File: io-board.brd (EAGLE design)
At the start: 76.2 x 75.9 mm, 26 parts

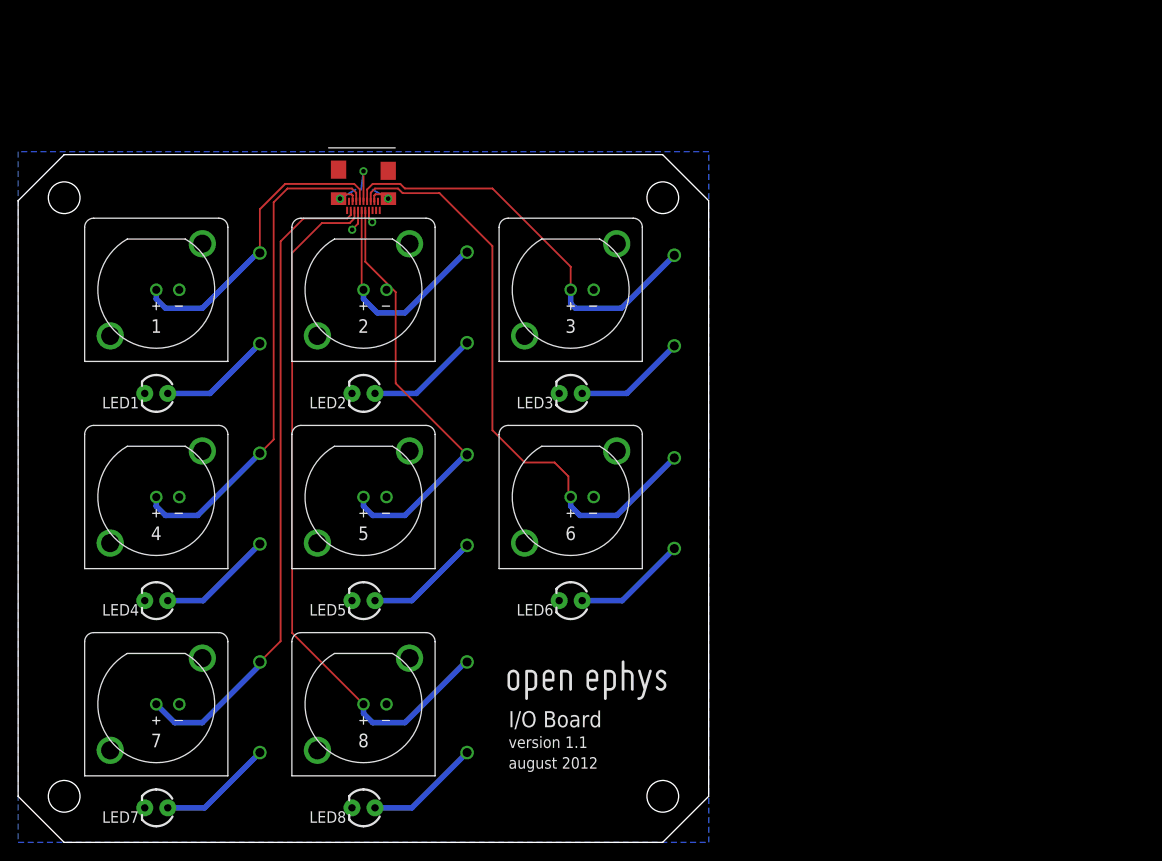
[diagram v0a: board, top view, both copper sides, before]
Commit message: Make rackmount board the default
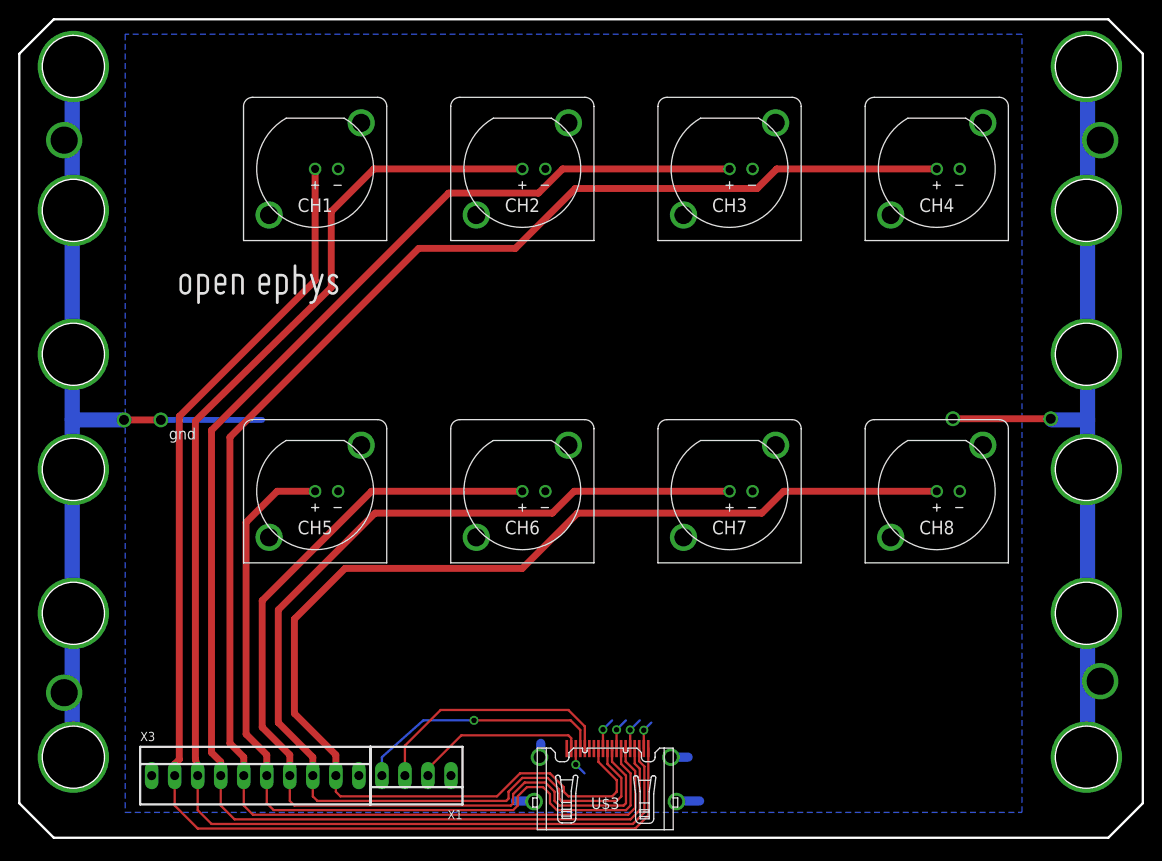
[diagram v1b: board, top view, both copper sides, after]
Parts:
- removed 1, 2, 3, 4, 5, 6, 7, 8: BNC_VERTICAL, josh:BNC_VERTICAL
- removed LED1, LED2, LED3, LED4, LED5, LED6, LED7, LED8: (no value), sparkfun:LED3MM
- removed R1, R2, R3, R4, R5, R6, R7, R8: RESISTOR_PTH, josh:RESISTOR_PTH
- removed U$1: (no value), voigts:MICRO_HDMI
- added CH1, CH2, CH3, CH4, CH5, CH6, CH7, CH8: BNC_VERTICAL, josh:BNC_VERTICAL
- added U$3: HDMI, open-ephys:HDMI_A
- added X1: 22-23-2041, con-molex:22-23-2041
- added X3: 22-23-2101, con-molex:22-23-2101
- moved U$2 56.7 mm to (17.1, 58.9)
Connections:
- removed net N$1: LED6.A, R6.P$2
- removed net N$10: LED1.A, R1.P$2
- removed net N$11: LED4.A, R4.P$2
- removed net N$12: LED7.A, R7.P$1
- removed net N$13: LED8.A, R8.P$1
- removed net N$14: LED2.A, R2.P$1
- removed net N$15: LED5.A, R5.P$1
- removed net N$6: 1.P$1, R1.P$1, U$1.PIN8
- removed net N$9: LED3.A, R3.P$2
- new net CH6: CH6.P$1, U$3.P$9, X3.7
- new net I2C_CLK: U$3.P$15, X1.3
- new net I2C_DAT: U$3.P$16, X1.4
- new net VCC: U$3.P$18, X1.2
- net DGND: now also CH1.P$2, CH2.P$2, CH3.P$2, CH4.P$2, CH5.P$2, CH6.P$2, CH7.P$2, CH8.P$2, U$3.P$11, U$3.P$17, U$3.P$2, U$3.P$5, U$3.P$8, X1.1, X3.1, X3.10; no longer 1.P$2, 2.P$2, 3.P$2, 4.P$2, 5.P$2, 6.P$2, 7.P$2, 8.P$2, LED1.K, LED2.K, LED3.K, LED4.K, LED5.K, LED6.K, LED7.K, LED8.K, U$1.PIN10, U$1.PIN13, U$1.PIN16, U$1.PIN4, U$1.PIN7
- net N$2: now also CH3.P$1, U$3.P$4, X3.4; no longer 8.P$1, R8.P$2, U$1.PIN5
- net N$23: now also CH4.P$1, U$3.P$6, X3.5; no longer 7.P$1, R7.P$2, U$1.PIN3
- net N$3: now also CH2.P$1, U$3.P$3, X3.3; no longer 2.P$1, R2.P$2, U$1.PIN9
- net N$4: now also CH1.P$1, U$3.P$1, X3.2; no longer 5.P$1, R5.P$2, U$1.PIN11
- net N$5: now also CH5.P$1, U$3.P$7, X3.6; no longer 4.P$1, R4.P$1, U$1.PIN6
- net N$7: now also CH7.P$1, U$3.P$10, X3.8; no longer 3.P$1, R3.P$1, U$1.PIN12
- net N$8: now also CH8.P$1, U$3.P$12, X3.9; no longer 6.P$1, R6.P$1, U$1.PIN14
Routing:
- net N$3: track 24.7 -> 153.1 mm
- net N$23: track 72.0 -> 182.4 mm
- net CH6: track 0.00 -> 104.7 mm
- net N$4: track 47.2 -> 137.9 mm
- net N$2: track 78.0 -> 165.2 mm
- net S$14: track 0.00 -> 76.2 mm
- net N$7: track 45.9 -> 120.9 mm
- net S$13: track 0.00 -> 73.9 mm
- net N$8: track 65.9 -> 137.1 mm
- net DGND: track 18.8 -> 56.6 mm, vias 5 -> 9
- net N$5: track 54.9 -> 91.6 mm
- net N$6: track 34.0 -> 0.00 mm, vias 0 -> 1
- net I2C_CLK: track 0.00 -> 28.0 mm
- net I2C_DAT: track 0.00 -> 28.0 mm, vias 0 -> 1
- net VCC: track 0.00 -> 19.6 mm
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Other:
- board size 76.2 x 75.9 mm -> 124 x 90.3 mm
- board text added: "1"
- board text added: "2"
- board text added: "3"
- board text added: "4"
- board text added: "5"
- board text added: "5vdc"
- board text added: "6"
- board text added: "7"
- board text added: "8"
- board text added: "8 7 6 5 4 3 2 1"
- board text added: "May 2013"
- board text added: "gnd"
- board text added: "i2c clk"
- board text added: "i2c dat"
- board text added: "version 1.3"
- board text removed: "august 2012"
- board text removed: "version 1.1"

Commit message: Add Illustrator file
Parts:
- renumbered U$3 to HDMI
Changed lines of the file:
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@@
 <element name="CH4" library="josh" package="BNC_VERTICAL" value="BNC_VERTICAL" x="101.346" y="74.295"/>
 <element name="U$2" library="josh" package="OPEN_EPHYS_LOGO" value="" x="17.145" y="58.928"/>
-<element name="U$3" library="open-ephys" package="HDMI_A" value="HDMI" x="64.77" y="9.398"/>
+<element name="HDMI" library="open-ephys" package="HDMI_A" value="HDMI" x="64.77" y="9.398"/>
 <element name="X1" library="con-molex" package="22-23-2041" value="22-23-2041" x="43.942" y="7.366" rot="R180">
 <attribute name="OC_NEWARK" value="38C0355" x="43.942" y="7.366" size="1.778" layer="27" rot="R180" display="off"/>
@@
 <signal name="N$2">
 <contactref element="CH3" pad="P$1"/>
-<contactref element="U$3" pad="P$4"/>
+<contactref element="HDMI" pad="P$4"/>
 <contactref element="X3" pad="4"/>
 <wire x1="78.486" y1="74.295" x2="60.071" y2="74.295" width="0.762" layer="1"/>
@@
 <signal name="N$3">
 <contactref element="CH2" pad="P$1"/>
-<contactref element="U$3" pad="P$3"/>
+<contactref element="HDMI" pad="P$3"/>
 <contactref element="X3" pad="3"/>
 <wire x1="55.626" y1="74.295" x2="39.243" y2="74.295" width="0.762" layer="1"/>
@@
 <signal name="N$4">
 <contactref element="CH1" pad="P$1"/>
-<contactref element="U$3" pad="P$1"/>
+<contactref element="HDMI" pad="P$1"/>
 <contactref element="X3" pad="2"/>
 <wire x1="32.766" y1="74.295" x2="32.766" y2="61.976" width="0.762" layer="1"/>
@@
 <signal name="N$5">
 <contactref element="CH5" pad="P$1"/>
-<contactref element="U$3" pad="P$7"/>
+<contactref element="HDMI" pad="P$7"/>
 <contactref element="X3" pad="6"/>
 <wire x1="32.766" y1="38.735" x2="28.575" y2="38.735" width="0.762" layer="1"/>
@@
 <signal name="CH6">
 <contactref element="CH6" pad="P$1"/>
-<contactref element="U$3" pad="P$9"/>
+<contactref element="HDMI" pad="P$9"/>
 <contactref element="X3" pad="7"/>
 <wire x1="65.52" y1="10.348" x2="65.532" y2="10.106" width="0.254" layer="1"/>
@@
 <signal name="N$7">
 <contactref element="CH7" pad="P$1"/>
-<contactref element="U$3" pad="P$10"/>
+<contactref element="HDMI" pad="P$10"/>
 <contactref element="X3" pad="8"/>
 <wire x1="78.486" y1="38.735" x2="61.341" y2="38.735" width="0.762" layer="1"/>
@@
 <signal name="N$8">
 <contactref element="CH8" pad="P$1"/>
-<contactref element="U$3" pad="P$12"/>
+<contactref element="HDMI" pad="P$12"/>
 <contactref element="X3" pad="9"/>
 <wire x1="101.346" y1="38.735" x2="84.455" y2="38.735" width="0.762" layer="1"/>
@@
 <contactref element="CH4" pad="P$2"/>
 <contactref element="CH8" pad="P$2"/>
-<contactref element="U$3" pad="P$2"/>
+<contactref element="HDMI" pad="P$2"/>
 <contactref element="CH3" pad="P$2"/>
 <contactref element="CH5" pad="P$2"/>
-<contactref element="U$3" pad="P$5"/>
+<contactref element="HDMI" pad="P$5"/>
 <contactref element="CH7" pad="P$2"/>
-<contactref element="U$3" pad="P$11"/>
+<contactref element="HDMI" pad="P$11"/>
 <contactref element="CH6" pad="P$2"/>
-<contactref element="U$3" pad="P$8"/>
-<contactref element="U$3" pad="P$17"/>
+<contactref element="HDMI" pad="P$8"/>
+<contactref element="HDMI" pad="P$17"/>
 <wire x1="57.658" y1="9.398" x2="57.658" y2="10.922" width="1.016" layer="16"/>
 <wire x1="56.896" y1="4.572" x2="54.864" y2="4.572" width="1.016" layer="16"/>
@@
 <signal name="N$23">
 <contactref element="CH4" pad="P$1"/>
-<contactref element="U$3" pad="P$6"/>
+<contactref element="HDMI" pad="P$6"/>
 <contactref element="X3" pad="5"/>
 <wire x1="101.346" y1="74.295" x2="83.693" y2="74.295" width="0.762" layer="1"/>
@@
 <signal name="VCC">
 <contactref element="X1" pad="2"/>
-<contactref element="U$3" pad="P$18"/>
+<contactref element="HDMI" pad="P$18"/>
 <wire x1="61.02" y1="10.348" x2="61.02" y2="11.497" width="0.254" layer="1"/>
 <wire x1="61.02" y1="11.497" x2="60.706" y2="11.811" width="0.254" layer="1"/>
@@
 <signal name="I2C_CLK">
 <contactref element="X1" pad="3"/>
-<contactref element="U$3" pad="P$15"/>
+<contactref element="HDMI" pad="P$15"/>
 <wire x1="62.52" y1="10.348" x2="62.52" y2="12.791" width="0.254" layer="1"/>
 <wire x1="62.52" y1="12.791" x2="60.706" y2="14.605" width="0.254" layer="1"/>
@@
 <signal name="I2C_DAT">
 <contactref element="X1" pad="4"/>
-<contactref element="U$3" pad="P$16"/>
+<contactref element="HDMI" pad="P$16"/>
 <wire x1="62.02" y1="10.348" x2="62.02" y2="12.402" width="0.254" layer="1"/>
 <wire x1="40.132" y1="7.366" x2="40.132" y2="9.398" width="0.254" layer="16"/>
@@
 </signal>
 <signal name="N$9">
-<via x="119.38" y="17.78" extent="1-16" drill="3" shape="square"/>
+<via x="119.38" y="16.51" extent="1-16" drill="3" shape="square"/>
 </signal>
 <signal name="N$10">
